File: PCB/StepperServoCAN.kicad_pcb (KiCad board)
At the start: 2 copper layers, 56 x 42.8 mm, 108 parts, among them J1 CAR, J2 Debug, J3 Motor, Q1 AO3401A, Q2 AO3401A, Q3 AO3400A, Q4 AO3400A, Q5 BSS84, SW1 Rst, SW2 Fcn>, U1 XL1509-adj, U10 LMV321, U2 TLE5012B, U3 SN65HVD230, U4 STM32F103CBT6, U5 A4950E, U6 A4950E, U8 LMV321, Y1 16Mhz 9pF

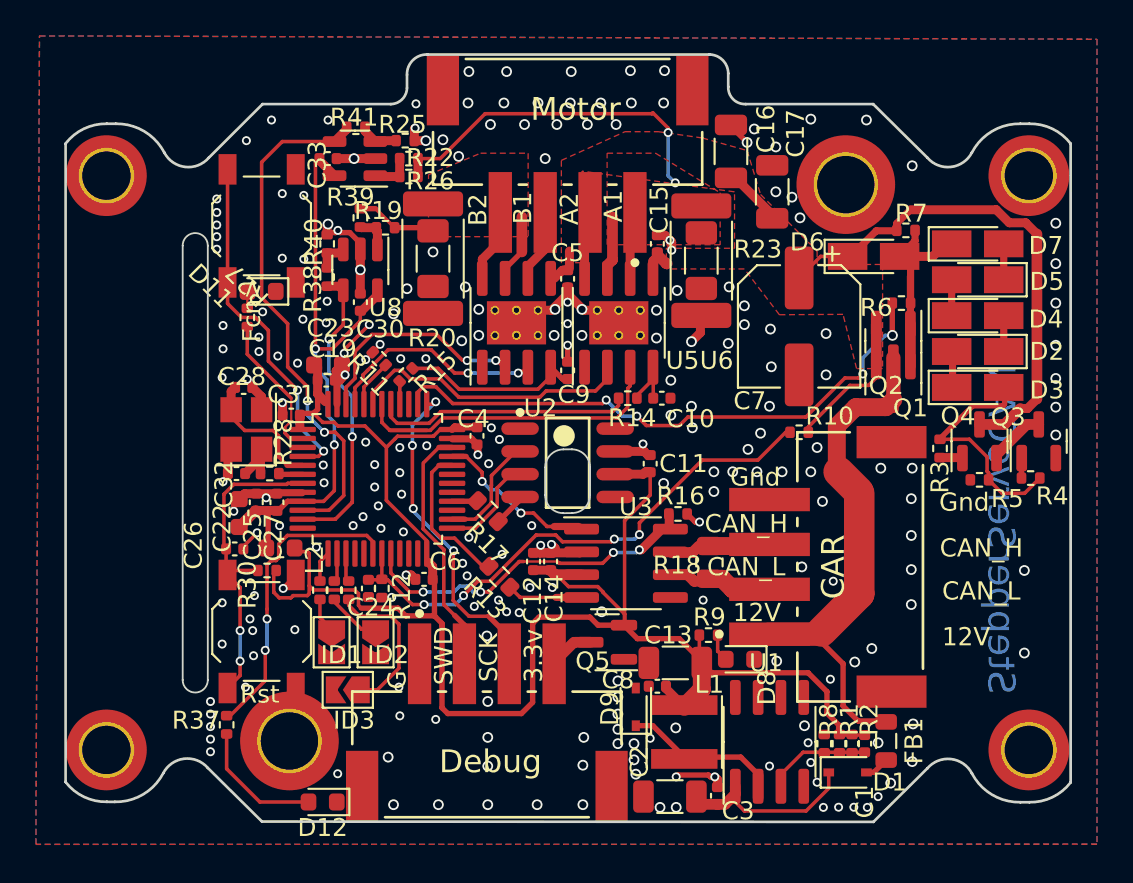
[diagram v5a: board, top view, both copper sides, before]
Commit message: Second edge cutout. Sharper corner cutouts
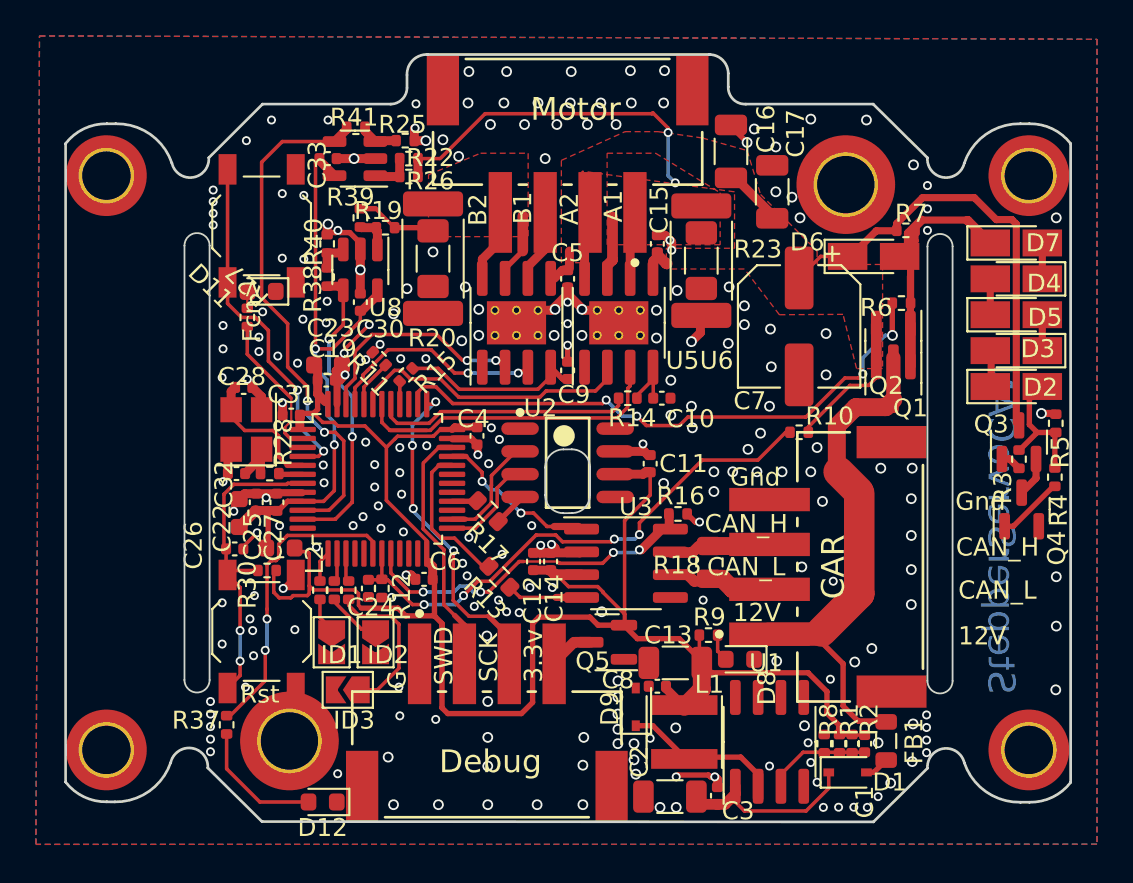
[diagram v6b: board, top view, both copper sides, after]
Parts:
- moved R5 5.29 mm to (127.2, 97.8), turned to -90 degrees
- moved R3 4.44 mm to (125.2, 99.8)
- moved Q4 3.92 mm to (125.3, 102.6)
- moved Q3 2.20 mm to (125.2, 98.8)
- moved D2 2.15 mm to (125.0, 95.8)
- moved D3 2.15 mm to (125.0, 93.8)
- moved D4 2.15 mm to (125.0, 89.8)
- moved D5 2.15 mm to (125.0, 91.8)
- moved D7 2.15 mm to (125.0, 87.8)
- moved R4 1.35 mm to (127.2, 100.8), turned to 90 degrees
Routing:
- net Net-(D2-Pad2): track 13.0 -> 7.50 mm
- net Net-(D6-Pad2): track 12.5 -> 16.1 mm
- net Net-(Q4-Pad1): track 1.12 -> 3.72 mm
- net VMOT: track 44.3 -> 41.7 mm
- net Net-(Q3-Pad2): track 3.24 -> 2.21 mm
- net GND: track 48.2 -> 49.0 mm, vias 234 -> 236
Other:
- outline, holes or cut-outs redrawn

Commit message: Connected TLE_IFA and TLE_IFB pins from angle sensor. Optimized routings
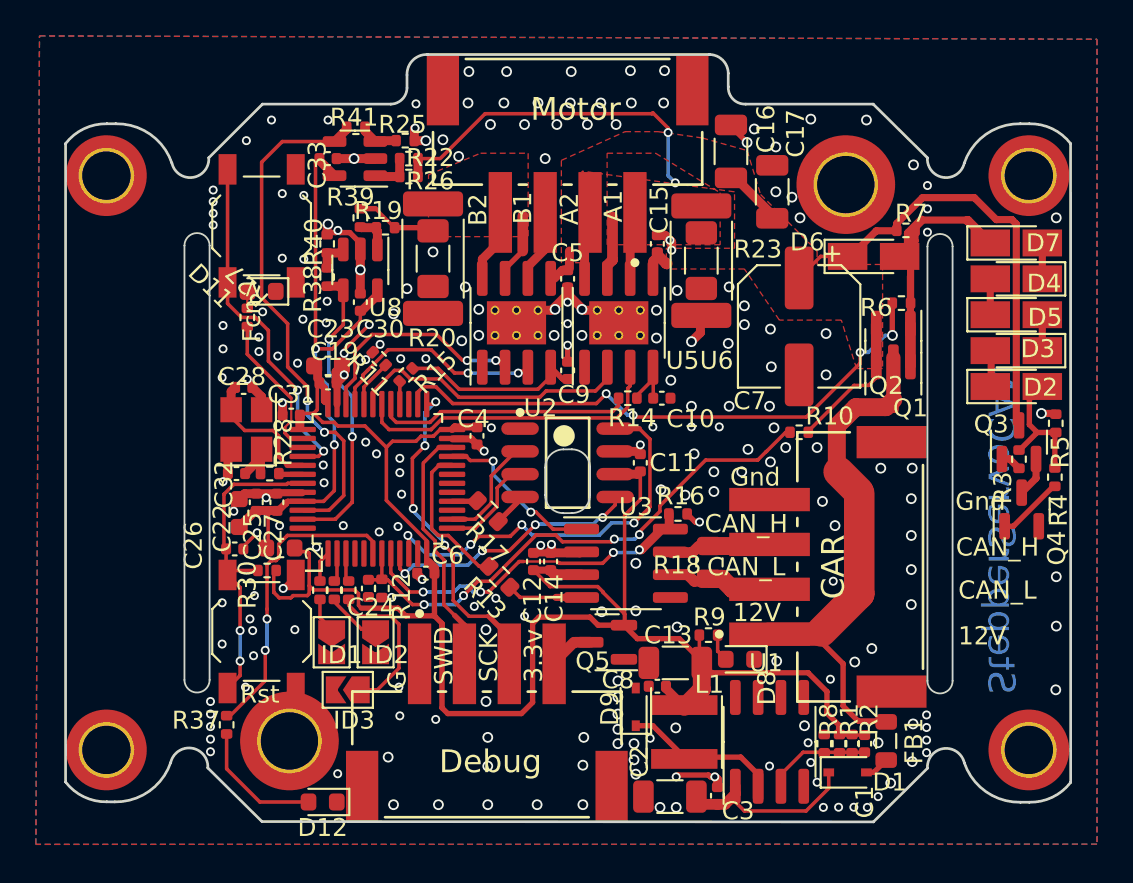
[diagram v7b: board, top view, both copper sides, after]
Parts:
- moved C11 0.55 mm to (104.0, 100.0)
- moved C6 0.36 mm to (92.1, 106.2)
- moved C19 0.19 mm to (86.7, 95.5)
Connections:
- U4 pad 21: unconnected-(U4-Pad21) -> TLE_IFA
- U4 pad 22: unconnected-(U4-Pad22) -> TLE_IFB
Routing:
- net TLE_IFB: track 0.00 -> 22.5 mm, vias 0 -> 4
- net TLE_IFA: track 0.00 -> 15.0 mm, vias 0 -> 4
- net A4950_A_IN1: track 19.8 -> 17.7 mm
- net GND: track 49.0 -> 47.5 mm, vias 236 -> 227

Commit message: Added second button
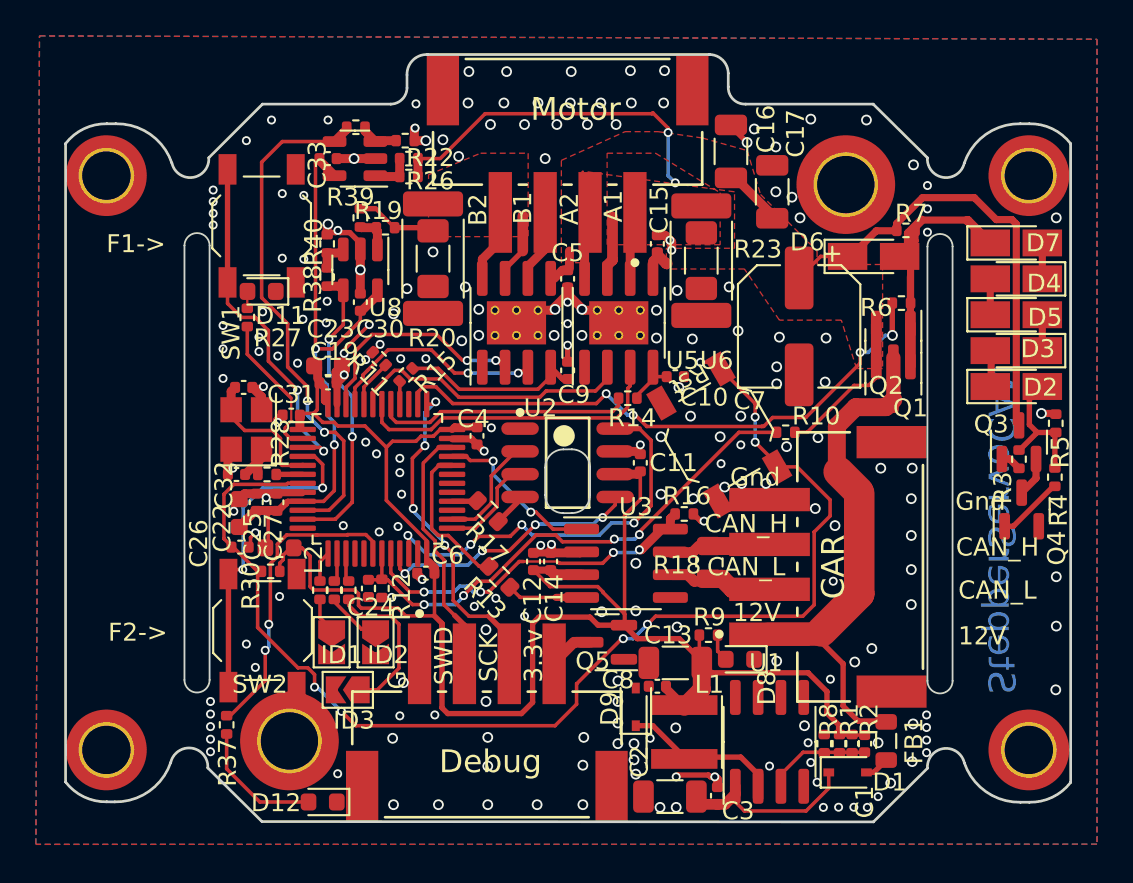
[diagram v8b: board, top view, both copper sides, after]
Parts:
- added SW2: Fcn>, Button_Switch_SMD:SW_SPST_TL3342, F.Cu at (83.0, 109.3)
- SW1: renamed from SW2; value Fcn> -> SW1
- moved SW3 27.8 mm to (108.5, 98.5), turned to 120 degrees
- moved C10 1.42 mm to (106.0, 95.2)
- moved R10 0.75 mm to (112.2, 98.3)
- moved R16 0.35 mm to (106.5, 102.8)
- moved C26 0.32 mm to (81.8, 104.7)
- moved R30 0.21 mm to (83.5, 106.0)
- moved R28 0.16 mm to (83.2, 100.7)
- moved L2 0.05 mm to (84.0, 104.7)
- moved C32 0.05 mm to (81.5, 100.7)
- renumbered SW1 to SW3
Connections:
- SW1 pad 1: /Switch -> Net-(U4-Pad3)
- U4 pad 3: unconnected-(U4-Pad3) -> Net-(U4-Pad3)
- U4 pad 4: /Switch -> Net-(U4-Pad4)
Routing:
- net NRST: track 18.2 -> 68.5 mm, vias 2 -> 7
- net /Switch: track 19.7 -> 0.00 mm, vias 2 -> 0
- net Net-(U4-Pad3): track 0.00 -> 19.6 mm, vias 0 -> 2
- net Net-(U4-Pad4): track 0.00 -> 18.2 mm, vias 0 -> 2
- net GND: track 47.5 -> 44.2 mm, vias 227 -> 211
- net +3.3V: track 102.7 -> 100.8 mm
- net VMOT_ADC: track 30.1 -> 29.1 mm
- net /Vref_A: track 3.68 -> 2.80 mm
- net VMOT: track 41.6 -> 42.3 mm
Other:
- board text added: "F1->"
- board text added: "F2->"
